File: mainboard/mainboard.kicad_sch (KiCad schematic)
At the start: 110 parts, among them IC1 TL084P, IC3 78L09, IC4 TL084P, T1 BC547, T2 BC557, T3 BC557, T4 BC557, T5 BC547, T6 BC557, T7 BC557, T8 BC557

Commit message: Schematic
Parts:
- removed C1, C11, C12, C2, C3, C7: 0.1 uf, mainboard:C050-030X075, symbol mainboard-eagle-import:C-US050-030X075
- removed C10, C5, C6, C9: 0.001, mainboard:C050-030X075, symbol mainboard-eagle-import:C-US050-030X075
- removed C13, C16, C17, C18, C4, C8: 10 uf, mainboard:C050-030X075, symbol mainboard-eagle-import:C-US050-030X075
- removed D1: 1N4001, mainboard:DO41-10, symbol mainboard-eagle-import:1N4004
- removed D2, D3, D4, D5, D6, D7, D8: (no value), symbol mainboard-eagle-import:ZENER-DIODEDO34-7
- removed IC1, IC4: TL084P, mainboard:DIL14, symbol mainboard-eagle-import:TL084P
- removed IC3: 78L09, mainboard:78LXX, symbol mainboard-eagle-import:78LXX
- removed LED1, LED3: (no value), mainboard:DO35-7, symbol mainboard-eagle-import:1N4148DO35-7
- removed LED2, LED4: 1N4148, mainboard:DO35-7, symbol mainboard-eagle-import:1N4148DO35-7
- removed OTA1, OTA3: LM13700N, mainboard:DIP16, symbol mainboard-eagle-import:LM13700N
- removed POWER0: 10_PIN_HEADER, mainboard:MA05-2, symbol mainboard-eagle-import:10_PIN_HEADER
- removed R1, R12, R15, R16, R19, R2, R22, R3, R4, R7, R8, R9: 47k, mainboard:0204_7, symbol mainboard-eagle-import:R-US_0204/7
- removed R10, R20, R47, R48, R49, R50, R51, R52: 470, mainboard:0204_7, symbol mainboard-eagle-import:R-US_0204/7
- removed R11, R13, R21, R23, R31, R40, R45, R46: 10k, mainboard:0204_7, symbol mainboard-eagle-import:R-US_0204/7
- removed R14, R32: 100k, mainboard:0204_7, symbol mainboard-eagle-import:R-US_0204/7
- removed R17, R18, R5, R6: 22k, mainboard:0204_7, symbol mainboard-eagle-import:R-US_0204/7
- removed R24, R29, R30, R33, R38, R39: 220k, mainboard:0204_7, symbol mainboard-eagle-import:R-US_0204/7
- removed R25, R27, R28, R34, R36, R37, R53, R54: 4.7k, mainboard:0204_7, symbol mainboard-eagle-import:R-US_0204/7
- removed R26, R35: 1m, mainboard:0204_7, symbol mainboard-eagle-import:R-US_0204/7
- removed R41, R42, R43, R44: 1k, mainboard:0204_7, symbol mainboard-eagle-import:R-US_0204/7
- removed T1, T5: BC547, mainboard:TO92, symbol mainboard-eagle-import:BC547
- removed T2, T3, T4, T6, T7, T8: BC557, mainboard:TO92-EBC, symbol mainboard-eagle-import:-PNP-TO92-EBC
- removed U$10, U$11, U$2, U$3, U$4, U$5, U$6, U$7, U$8, U$9: (no value), symbol mainboard-eagle-import:WQP-PJ301M-12_JACK
- removed VR1, VR2, VR4, VR5: 25k, mainboard:EVUFXL, symbol mainboard-eagle-import:EVUL
- added C1, C12, C13, C14, C2, C3: 100nF, Capacitor_THT:C_Axial_L3.8mm_D2.6mm_P7.50mm_Horizontal, symbol Device:C
- added C10, C11, C7, C8: 1nF, Capacitor_THT:C_Disc_D5.0mm_W2.5mm_P5.00mm, symbol Device:C
- added C4, C5, C6, C9: 10uF, Capacitor_THT:CP_Radial_D5.0mm_P2.50mm, symbol Device:C_Polarized
- added D1, D3: BAT85, Diode_THT:D_DO-35_SOD27_P7.62mm_Horizontal, symbol Diode:BAT85
- added D2: 1N4001, Diode_THT:D_DO-41_SOD81_P10.16mm_Horizontal, symbol Diode:1N4001
- added J1: CV-A, winterbloom:AudioJack_WQP518MA, symbol winterbloom:Eurorack_Mono_Jack
- added J2: In-A, winterbloom:AudioJack_WQP518MA, symbol winterbloom:Eurorack_Mono_Jack
- added J3: In-AB, winterbloom:AudioJack_WQP518MA, symbol winterbloom:Eurorack_Mono_Jack
- added J4: In-B, winterbloom:AudioJack_WQP518MA, symbol winterbloom:Eurorack_Mono_Jack
- added J5: Eurorack_Power, winterbloom:Eurorack_Power_2x5_Shrouded, symbol winterbloom:Eurorack_Power
- added J6: CV-B, winterbloom:AudioJack_WQP518MA, symbol winterbloom:Eurorack_Mono_Jack
- added J7: Out-A, winterbloom:AudioJack_WQP518MA, symbol winterbloom:Eurorack_Mono_Jack
- added J8: Out-AB, winterbloom:AudioJack_WQP518MA, symbol winterbloom:Eurorack_Mono_Jack
- added J9: Out-B, winterbloom:AudioJack_WQP518MA, symbol winterbloom:Eurorack_Mono_Jack
- added Q1, Q5: BC547, Package_TO_SOT_THT:TO-92_Inline, symbol Transistor_BJT:BC547
- added Q2, Q3, Q4, Q6, Q7, Q8: BC557, Package_TO_SOT_THT:TO-92_Inline, symbol Transistor_BJT:BC557
- added R1, R15, R2, R26, R27, R43: 220k, Resistor_THT:R_Axial_DIN0204_L3.6mm_D1.6mm_P7.62mm_Horizontal, symbol Device:R
- added R10, R13, R14, R16, R17, R33, R34, R5, R6, R7, R9: 47k, Resistor_THT:R_Axial_DIN0204_L3.6mm_D1.6mm_P7.62mm_Horizontal, symbol Device:R
- added R11, R12, R28, R29, R3, R39, R4, R42: 4.7k, Resistor_THT:R_Axial_DIN0204_L3.6mm_D1.6mm_P7.62mm_Horizontal, symbol Device:R
- added R18, R19, R20, R21, R35, R36, R37, R38: 470, Resistor_THT:R_Axial_DIN0204_L3.6mm_D1.6mm_P7.62mm_Horizontal, symbol Device:R
- added R22, R23: 100k, Resistor_THT:R_Axial_DIN0204_L3.6mm_D1.6mm_P7.62mm_Horizontal, symbol Device:R
- added R24, R25, R40, R41, R46, R47, R48, R49: 10k, Resistor_THT:R_Axial_DIN0204_L3.6mm_D1.6mm_P7.62mm_Horizontal, symbol Device:R
- added R30, R8: 1Meg, Resistor_THT:R_Axial_DIN0204_L3.6mm_D1.6mm_P7.62mm_Horizontal, symbol Device:R
- added R31, R32, R44, R45: 22k, Resistor_THT:R_Axial_DIN0204_L3.6mm_D1.6mm_P7.62mm_Horizontal, symbol Device:R
- added RV1: CUT-A, winterbloom:Potentiometer_Alpha_R0904N, symbol winterbloom:Eurorack_Pot
- added RV2: CV-A, winterbloom:Potentiometer_Alpha_R0904N, symbol winterbloom:Eurorack_Pot
- added RV3: Res-A, winterbloom:Potentiometer_Alpha_R0904N, symbol winterbloom:Eurorack_Pot
- added RV4: Res-B, winterbloom:Potentiometer_Alpha_R0904N, symbol winterbloom:Eurorack_Pot
- added RV5: CUT-B, winterbloom:Potentiometer_Alpha_R0904N, symbol winterbloom:Eurorack_Pot
- added RV6: CV-B, winterbloom:Potentiometer_Alpha_R0904N, symbol winterbloom:Eurorack_Pot
- added U1: L78L09_TO92, Package_TO_SOT_THT:TO-92_Inline, symbol Regulator_Linear:L78L09_TO92
- added U2, U3: TL084, Package_DIP:DIP-14_W7.62mm_Socket, symbol Amplifier_Operational:TL084
- added U4, U5: LM13700, Package_DIP:DIP-16_W7.62mm_Socket, symbol Amplifier_Operational:LM13700
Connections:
- net GND: now also C4.2, C5.2, C6.2, C9.2, D1.2 (A), D3.2 (A), J1.S (Sleeve), J2.S (Sleeve), J3.S (Sleeve), J4.S (Sleeve), J5.3 (GND), J5.4 (GND), J5.5 (GND), J5.6 (GND), J5.7 (GND), J5.8 (GND), J6.S (Sleeve), J7.S (Sleeve), J8.S (Sleeve), J9.S (Sleeve), R11.1, R15.2, R30.1, R32.2, R39.1, R43.2, R45.2, R8.1, RV1.1, RV2.1, RV5.1, RV6.1, U2.11 (V-), U3.11 (V-), U4.6 (V-), U5.6 (V-)
- net MIDO1: now also R12.1, R18.1, R19.2, R35.1, R36.2, R4.1, RV3.1, U2.1, U2.10 (+), U2.12 (+), U2.2 (-)
- net MIDO2: now also R20.1, R21.2, R29.1, R37.1, R38.2, R42.1, RV4.1, U3.1, U3.10 (+), U3.12 (+), U3.2 (-)
- new net: R41.1, U5.1
- new net: R34.1, R38.1, U5.3 (+)
- new net: R37.2, U5.4 (-)
- new net: C11.1, U3.13 (-), U5.5
- new net: C2.1, J3.T (Tip)
- new net: C2.2, R6.1
- new net: Q4.2 (B), R12.2, R15.1
- new net: C1.1, J2.T (Tip)
- new net: C1.2, R5.1
- new net: C4.1, D2.1 (K), U1.3 (VI)
- new net: Q8.2 (B), R42.2, R43.1
- new net: R23.1, RV4.3
- new net: C8.2, R23.2, R34.2, U3.8
- new net: D2.2 (A), J5.10 (+12V), J5.9 (+12V)
- new net: Q1.2 (B), R1.2, R3.1
- new net: R17.1, R21.1, U5.14 (+)
- new net: Q5.2 (B), R26.2, R28.1
- new net: D1.1 (K), J1.T (Tip), RV2.3
- new net: Q1.3 (E), Q3.2 (B), R8.2
- new net: R25.1, U5.16
- new net: Q2.2 (B), R2.2, R4.2
- new net: Q2.3 (E), Q3.1 (C), Q4.3 (E)
- new net: C6.1, R31.2, R32.1, U2.3 (+)
- new net: C9.1, R44.2, R45.1, U3.3 (+)
- new net: R26.1, RV5.2
- new net: C13.1, R47.1, R48.1
- new net: C13.2, J8.T (Tip)
- new net: R27.1, RV6.2
- new net: Q6.2 (B), R27.2, R29.2
- new net: R10.1, R13.2, R14.2, R5.2, R6.2, R7.2, R9.1, U2.6 (-), U3.6 (-)
- new net: C10.2, R46.2, R47.2, R9.2, U2.14
- new net: R2.1, RV2.2
- new net: R22.1, RV3.3
- new net: C7.2, R22.2, R33.2, U2.8
- new net: C14.1, R49.1
- new net: C11.2, R10.2, R48.2, R49.2, U3.14
- new net: R33.1, R36.1, U4.3 (+)
- new net: R40.1, U4.1
- new net: RV4.2, U3.5 (+)
- new net: R14.1, R17.2, U3.7
- new net: C14.2, J9.T (Tip)
- new net: R13.1, R16.2, U2.7
- new net: C8.1, U3.9 (-), U5.12
- new net: Q6.3 (E), Q7.1 (C), Q8.3 (E)
- new net: Q5.3 (E), Q7.2 (B), R30.2
- new net: R1.1, RV1.2
- new net: RV3.2, U2.5 (+)
- new net: D3.1 (K), J6.T (Tip), RV6.3
- new net: Q8.1 (C), R39.2
- new net: C3.1, J4.T (Tip)
- new net: C3.2, R7.1
- new net: R20.2, U5.13 (-)
- new net: C7.1, U2.9 (-), U4.12
- new net: C12.1, R46.1
- new net: J5.1 (-12V), J5.2 (-12V)
- new net: C10.1, U2.13 (-), U4.5
- new net: R35.2, U4.4 (-)
- new net: R24.1, U4.16
- new net: Q4.1 (C), R11.2
- new net: R16.1, R19.1, U4.14 (+)
- new net: R18.2, U4.13 (-)
- new net: C12.2, J7.T (Tip)
- new net +9V: C5.1, J1.TN (Tip_normalize), J6.TN (Tip_normalize), Q1.1 (C), Q3.3 (E), Q5.1 (C), Q7.3 (E), R28.2, R3.2, R31.1, R44.1, RV1.3, RV5.3, U1.1 (VO), U2.4 (V+), U3.4 (V+), U4.11 (V+), U5.11 (V+)
- new net VC1: Q2.1 (C), R24.2, R40.2
- new net VC2: Q6.1 (C), R25.2, R41.2
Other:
- note added: "CV1"
- note added: "CV2"
- note added: "Filter 1"
- note added: "Filter 2"
- note added: "Power"

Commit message: Panel and trace corrections
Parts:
- added R50: 47k, Resistor_THT:R_Axial_DIN0204_L3.6mm_D1.6mm_P7.62mm_Horizontal, symbol Device:R
- U2, U3: value TL084 -> (none); footprint Package_DIP:DIP-14_W7.62mm_Socket -> (none)
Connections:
- net GND: now also U1.2 (GND)
- net MIDO1: now also U2.5 (+); no longer U2.12 (+)
- net MIDO2: now also U3.5 (+); no longer U3.12 (+)
- net at C11.1, U5.5: now also U3.6 (-); no longer U3.13 (-)
- net at C2.2, R6.1: now also R50.1
- net at C10.2, R46.2, R47.2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: now also U2.7; no longer U2.14
- net at C11.2, R10.2, R48.2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: now also U3.7; no longer U3.14
- net at RV4.2: now also U3.12 (+); no longer U3.5 (+)
- net at R14.1, R17.2: now also U3.14; no longer U3.7
- net at R13.1, R16.2: now also U2.14; no longer U2.7
- net at RV3.2: now also U2.12 (+); no longer U2.5 (+)
- net at C10.1, U4.5: now also U2.6 (-); no longer U2.13 (-)
- new net: R13.2, R5.2, R50.2, R9.1, U2.13 (-)
- new net: R10.1, R14.2, R6.2, R7.2, U3.13 (-)
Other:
- moved on the sheet: C1, C12, C3, J2, J4, J7, R10, R14, R16, R17, R18, R19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

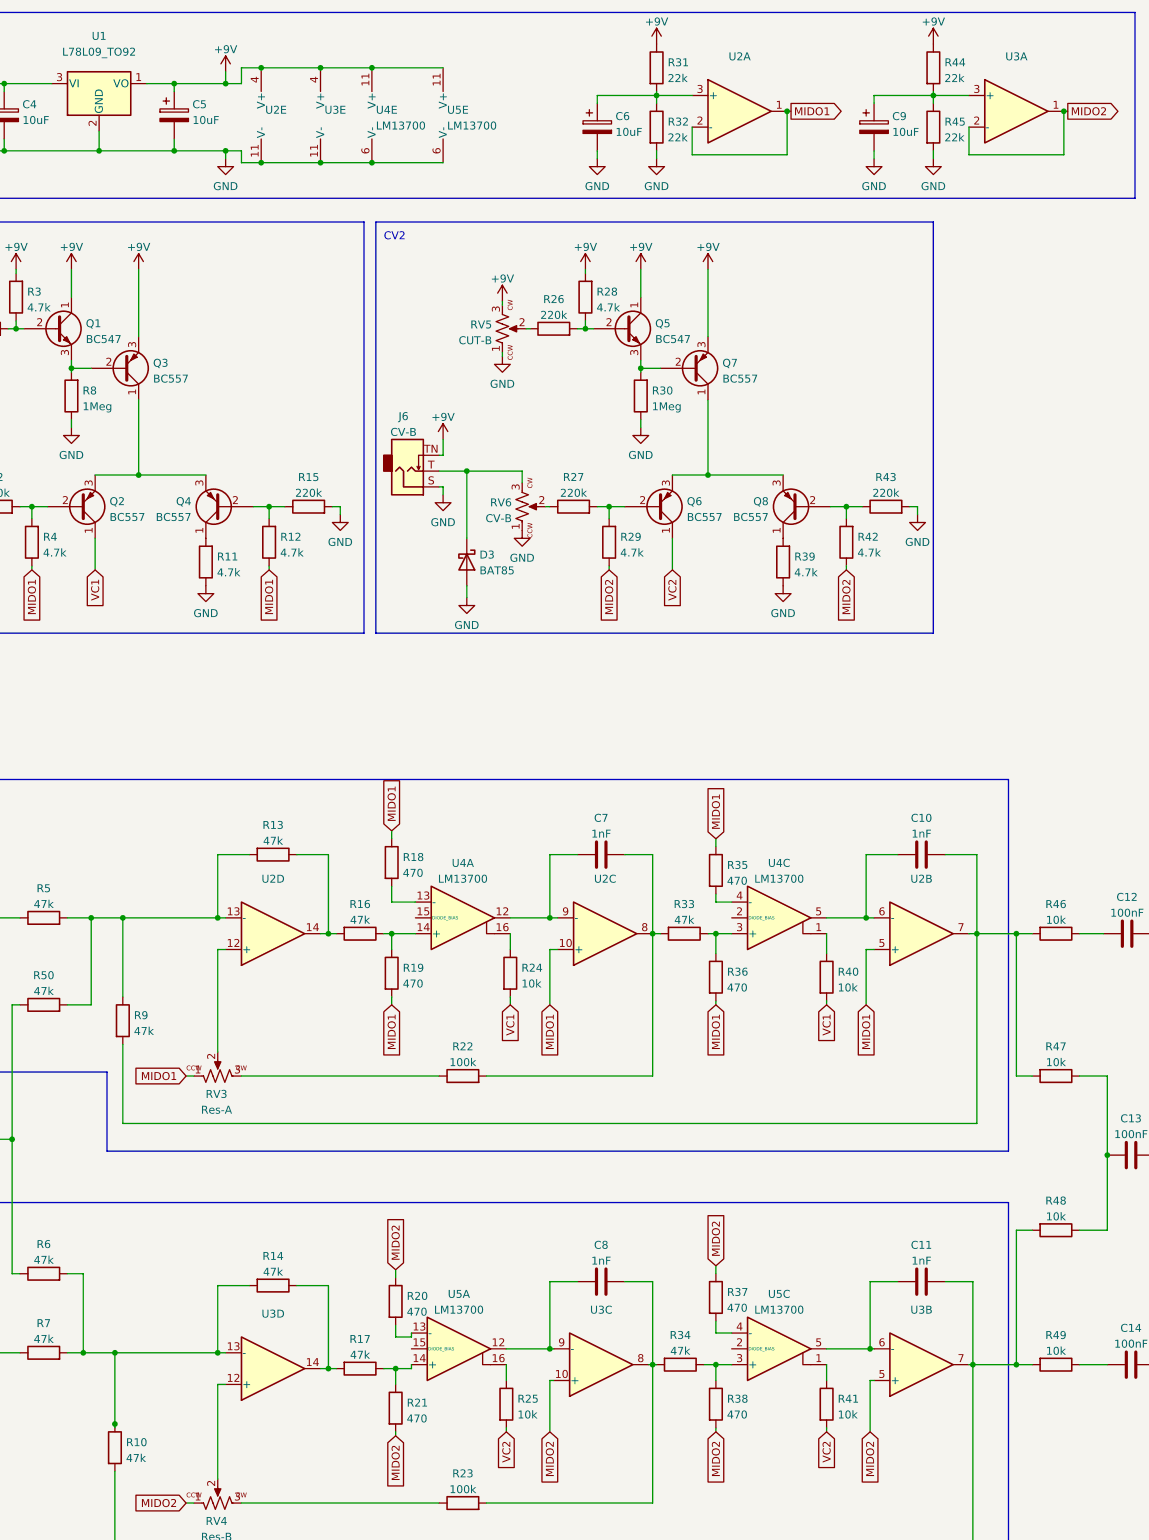
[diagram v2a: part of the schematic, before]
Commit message: updated BOM, some layout tweaks
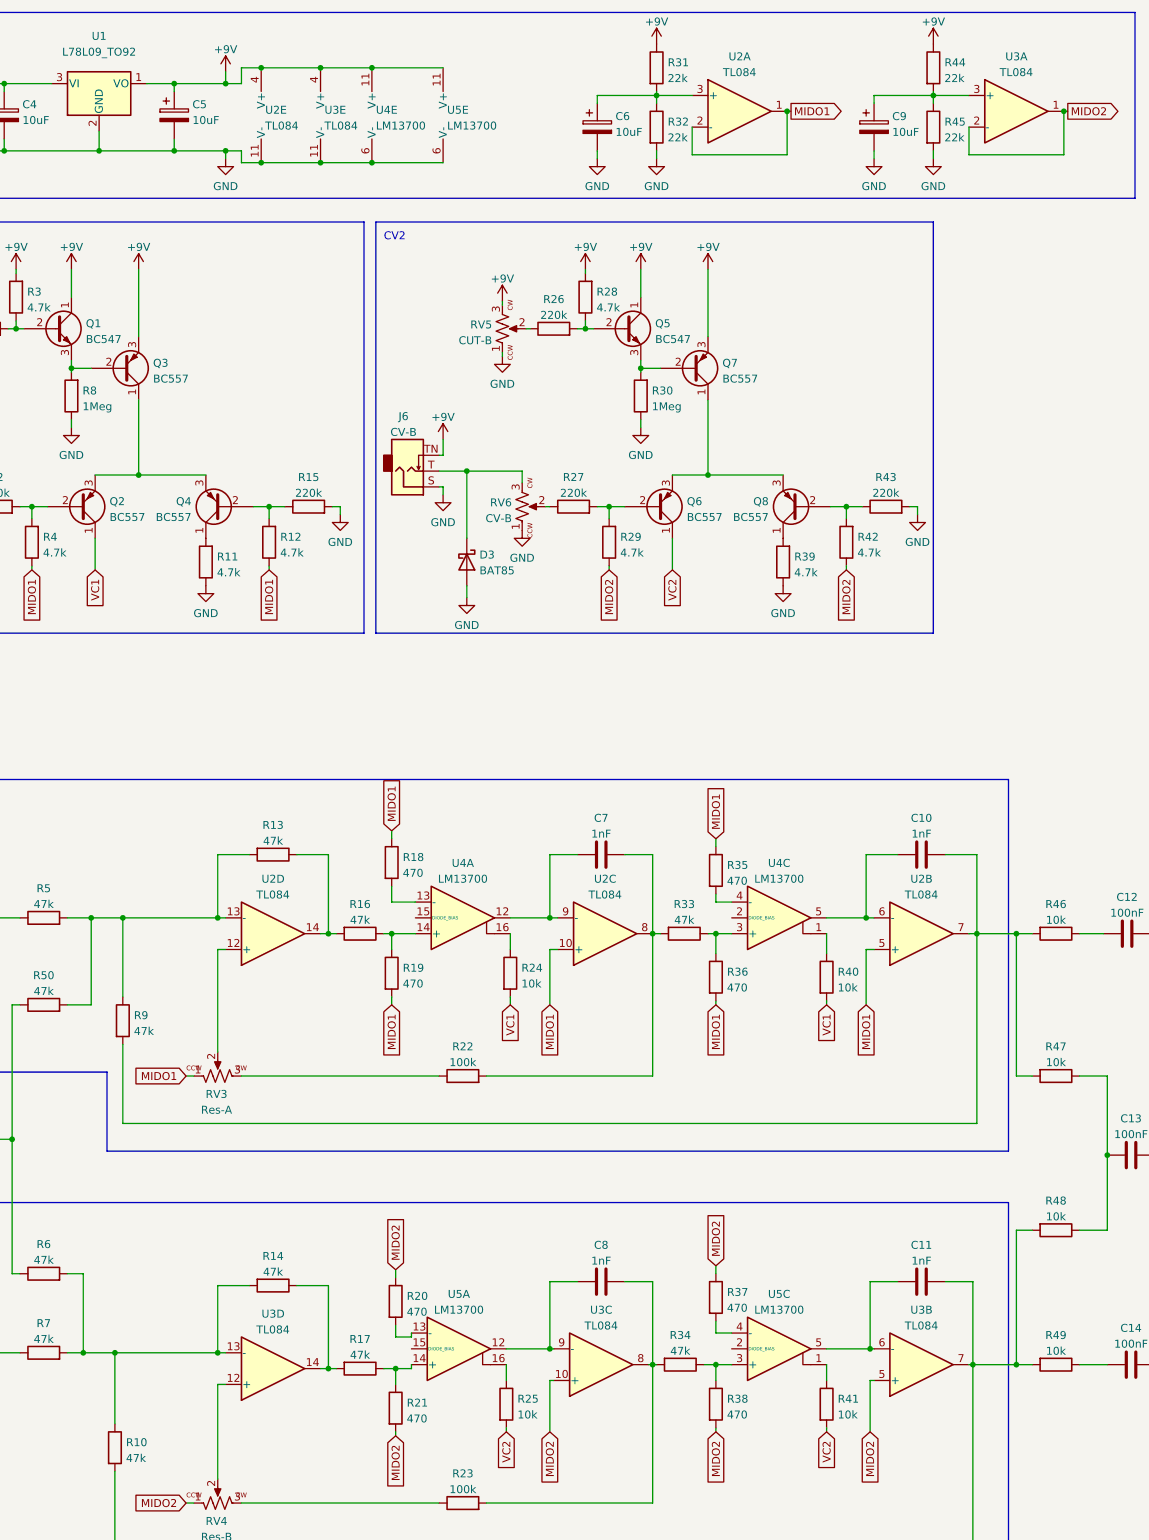
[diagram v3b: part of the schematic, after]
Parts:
- U2, U3: value (none) -> TL084; footprint (none) -> Package_DIP:DIP-14_W7.62mm_Socket
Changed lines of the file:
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@@
   (junction (at 151.13 230.505) (diameter 0) (color 0 0 0 0)
   )
-  (junction (at 64.77 240.03) (diameter 0) (color 0 0 0 0)
-  )
   (junction (at 88.265 37.465) (diameter 0) (color 0 0 0 0)
   )
@@
     (stroke (width 0) (type default) (color 0 0 0 0))
   )
-  (wire (pts (xy 64.77 240.665) (xy 64.77 240.03))
-    (stroke (width 0) (type default) (color 0 0 0 0))
-  )
   (wire (pts (xy 116.84 86.995) (xy 121.285 86.995))
     (stroke (width 0) (type default) (color 0 0 0 0))
@@
     (in_bom yes) (on_board yes) (fields_autoplaced)
     (property "Reference" "U3" (id 0) (at 209.55 20.4302 0))
-    (property "Value" "" (id 1) (at 209.55 22.9671 0))
-    (property "Footprint" "" (id 2) (at 208.28 26.67 0)
+    (property "Value" "TL084" (id 1) (at 209.55 22.9671 0))
+    (property "Footprint" "Package_DIP:DIP-14_W7.62mm_Socket" (id 2) (at 208.28 26.67 0)
       (effects (font (size 1.27 1.27)) hide)
     )
@@
     (in_bom yes) (on_board yes) (fields_autoplaced)
     (property "Reference" "U3" (id 0) (at 90.17 222.3602 0))
-    (property "Value" "" (id 1) (at 90.17 224.8971 0))
-    (property "Footprint" "" (id 2) (at 88.9 233.68 0)
+    (property "Value" "TL084" (id 1) (at 90.17 224.8971 0))
+    (property "Footprint" "Package_DIP:DIP-14_W7.62mm_Socket" (id 2) (at 88.9 233.68 0)
       (effects (font (size 1.27 1.27)) hide)
     )
@@
     (in_bom yes) (on_board yes) (fields_autoplaced)
     (property "Reference" "U2" (id 0) (at 165.1 20.4302 0))
-    (property "Value" "" (id 1) (at 165.1 22.9671 0))
-    (property "Footprint" "" (id 2) (at 163.83 26.67 0)
+    (property "Value" "TL084" (id 1) (at 165.1 22.9671 0))
+    (property "Footprint" "Package_DIP:DIP-14_W7.62mm_Socket" (id 2) (at 163.83 26.67 0)
       (effects (font (size 1.27 1.27)) hide)
     )
@@
     (in_bom yes) (on_board yes) (fields_autoplaced)
     (property "Reference" "U2" (id 0) (at 90.17 152.5102 0))
-    (property "Value" "" (id 1) (at 90.17 155.0471 0))
-    (property "Footprint" "" (id 2) (at 88.9 163.83 0)
+    (property "Value" "TL084" (id 1) (at 90.17 155.0471 0))
+    (property "Footprint" "Package_DIP:DIP-14_W7.62mm_Socket" (id 2) (at 88.9 163.83 0)
       (effects (font (size 1.27 1.27)) hide)
     )
@@
     (in_bom yes) (on_board yes) (fields_autoplaced)
     (property "Reference" "U3" (id 0) (at 194.31 221.7252 0))
-    (property "Value" "" (id 1) (at 194.31 224.2621 0))
-    (property "Footprint" "" (id 2) (at 193.04 233.045 0)
+    (property "Value" "TL084" (id 1) (at 194.31 224.2621 0))
+    (property "Footprint" "Package_DIP:DIP-14_W7.62mm_Socket" (id 2) (at 193.04 233.045 0)
       (effects (font (size 1.27 1.27)) hide)
     )
@@
     (in_bom yes) (on_board yes) (fields_autoplaced)
     (property "Reference" "U3" (id 0) (at 142.875 221.7252 0))
-    (property "Value" "" (id 1) (at 142.875 224.2621 0))
-    (property "Footprint" "" (id 2) (at 141.605 233.045 0)
+    (property "Value" "TL084" (id 1) (at 142.875 224.2621 0))
+    (property "Footprint" "Package_DIP:DIP-14_W7.62mm_Socket" (id 2) (at 141.605 233.045 0)
       (effects (font (size 1.27 1.27)) hide)
     )
@@
       (effects (font (size 1.27 1.27)) (justify left))
     )
-    (property "Value" "" (id 1) (at 88.9 31.5472 0)
+    (property "Value" "TL084" (id 1) (at 88.9 31.5472 0)
       (effects (font (size 1.27 1.27)) (justify left))
     )
-    (property "Footprint" "" (id 2) (at 89.535 27.305 0)
+    (property "Footprint" "Package_DIP:DIP-14_W7.62mm_Socket" (id 2) (at 89.535 27.305 0)
       (effects (font (size 1.27 1.27)) hide)
     )
@@
       (effects (font (size 1.27 1.27)) (justify left))
     )
-    (property "Value" "" (id 1) (at 98.425 31.5472 0)
+    (property "Value" "TL084" (id 1) (at 98.425 31.5472 0)
       (effects (font (size 1.27 1.27)) (justify left))
     )
-    (property "Footprint" "" (id 2) (at 99.06 27.305 0)
+    (property "Footprint" "Package_DIP:DIP-14_W7.62mm_Socket" (id 2) (at 99.06 27.305 0)
       (effects (font (size 1.27 1.27)) hide)
     )
@@
     (in_bom yes) (on_board yes) (fields_autoplaced)
     (property "Reference" "U2" (id 0) (at 194.31 152.5102 0))
-    (property "Value" "" (id 1) (at 194.31 155.0471 0))
-    (property "Footprint" "" (id 2) (at 193.04 163.83 0)
+    (property "Value" "TL084" (id 1) (at 194.31 155.0471 0))
+    (property "Footprint" "Package_DIP:DIP-14_W7.62mm_Socket" (id 2) (at 193.04 163.83 0)
       (effects (font (size 1.27 1.27)) hide)
     )
@@
     (in_bom yes) (on_board yes) (fields_autoplaced)
     (property "Reference" "U2" (id 0) (at 143.51 152.5102 0))
-    (property "Value" "" (id 1) (at 143.51 155.0471 0))
-    (property "Footprint" "" (id 2) (at 142.24 163.83 0)
+    (property "Value" "TL084" (id 1) (at 143.51 155.0471 0))
+    (property "Footprint" "Package_DIP:DIP-14_W7.62mm_Socket" (id 2) (at 142.24 163.83 0)
       (effects (font (size 1.27 1.27)) hide)
     )
